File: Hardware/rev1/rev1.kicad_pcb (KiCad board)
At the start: 2 copper layers, 13 parts, among them J1 USB_C_Receptacle_GCT_USB4085, J3 TerminalBlock_MetzConnect_360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, U1 - STM32F103 LQFP-48, U2 SOT-89-3, U3 LGA-8, U4 SOIC-8, Y1 Crystal_SMD

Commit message: hehe did something lol
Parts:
- added C8: C_0402, Capacitor_SMD:C_0402_1005Metric, F.Cu at (117.2, 103.2)
- added C9: C_0402, Capacitor_SMD:C_0402_1005Metric, F.Cu at (126.0, 98.6)
- added D1: D_0402_1005Metric, Diode_SMD:D_0402_1005Metric, F.Cu at (125.6, 94.8)
- added D2: D_0402_1005Metric, Diode_SMD:D_0402_1005Metric, F.Cu at (116.0, 96.8)
- moved GND 77.5 mm to (158.0, 97.3), turned to -90 degrees
- moved J1 64.9 mm to (111.1, 96.0), turned to -90 degrees
- moved R2 59.2 mm to (113.2, 97.8), turned to 180 degrees
- moved R4 56.7 mm to (113.2, 99.4), turned to 180 degrees
- moved C11 44.2 mm to (147.9, 102.3)
- moved U3 42.6 mm to (150.4, 103.5)
- moved R6 37.9 mm to (154.1, 101.4), turned to 180 degrees
- moved R7 35.8 mm to (154.1, 103.2), turned to 180 degrees
- moved J3 32.0 mm to (122.0, 96.2), turned to 180 degrees
- moved U4 25.5 mm to (131.2, 100.7)
- moved U2 24.9 mm to (120.5, 101.4), turned to 90 degrees
- moved U1 - STM32F103 12.7 mm to (141.1, 99.3)
- moved Y1 11.4 mm to (153.6, 98.4)
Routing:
- net (no net): track 165.5 -> 164.8 mm, vias 3 -> 4

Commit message: who actually knows what i have done, daniel says most of it needs work lol
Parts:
- removed C11, C8, C9: C_0402, Capacitor_SMD:C_0402_1005Metric
- removed D1, D2: D_0402_1005Metric, Diode_SMD:D_0402_1005Metric
- removed GND: Battery_Panasonic_CR1025-VSK_Vertical_CircularHoles, Battery:Battery_Panasonic_CR1025-VSK_Vertical_CircularHoles
- removed U1 - STM32F103: LQFP-48, Package_QFP:LQFP-48_7x7mm_P0.5mm
- added C12: 10p, Capacitor_SMD:C_0402_1005Metric, F.Cu at (148.6, 58.7)
- added C13: 10p, Capacitor_SMD:C_0402_1005Metric, F.Cu at (151.2, 62.1)
- added R1: 1k5, Resistor_SMD:R_0402_1005Metric, F.Cu at (123.9, 60.1)
- added R5: 1k5, Resistor_SMD:R_0402_1005Metric, F.Cu at (147.3, 93.4)
- added REF**: BatteryHolder_Keystone_3034_1x20mm, Battery:BatteryHolder_Keystone_3034_1x20mm, B.Cu at (136.8, 109.0)
- added U1: STM32F103C8Tx, Package_QFP:LQFP-48_7x7mm_P0.5mm, F.Cu at (137.0, 109.2)
- J1: value USB_C_Receptacle_GCT_USB4085 -> USB_C_Receptacle_GCT_USB4105-xx-A_16P_TopMnt_Horizontal; footprint Connector_USB:USB_C_Receptacle_GCT_USB4085 -> Connector_USB:USB_C_Receptacle_GCT_USB4105-xx-A_16P_TopMnt_Horizontal
- R2, R4: value R_0402 -> 5k1
- R6, R7: value R_0603 -> 10k; footprint Resistor_SMD:R_0603_1608Metric -> Resistor_SMD:R_0402_1005Metric
- U2: value SOT-89-3 -> HT75xx-1-SOT89
- U3: value LGA-8 -> MS5607-02BA
- U4: value SOIC-8 -> W25Q128JVS
- Y1: value Crystal_SMD -> 16MHz
- moved J1 48.1 mm to (153.8, 118.2), turned to 0 degrees
- moved U3 45.6 mm to (111.6, 79.5)
- moved R2 44.5 mm to (122.3, 54.3), turned to 0 degrees
- moved R7 42.7 mm to (118.3, 79.8), turned to 0 degrees
- moved R6 40.4 mm to (121.9, 77.0), turned to 0 degrees
- moved Y1 40.1 mm to (143.0, 59.7)
- moved R4 33.9 mm to (135.9, 74.3), turned to 0 degrees
- moved U4 33.7 mm to (115.3, 71.0), turned to 0 degrees
- moved J3 31.2 mm to (152.6, 102.1), turned to 0 degrees
- moved U2 29.3 mm to (145.8, 116.3), turned to -90 degrees
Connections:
- R2 pad 1: (no net) -> GND
- R2 pad 2: (no net) -> Net-(J1-CC1)
- R4 pad 1: (no net) -> Net-(J1-CC2)
- R4 pad 2: (no net) -> GND
- R6 pad 1: (no net) -> +3.3V
- R6 pad 2: (no net) -> I2C2_SDA
- R7 pad 1: (no net) -> +3.3V
- R7 pad 2: (no net) -> I2C2_SCK
- U2 pad 1: (no net) -> GND
- U2 pad 2: (no net) -> Net-(J3-Pin_2)
- U2 pad 3: (no net) -> +3V3
- U3 pad 1: (no net) -> +3.3V
- U3 pad 2: (no net) -> +3.3V
- U3 pad 3: (no net) -> GND
- U3 pad 4: (no net) -> GND
- U3 pad 5: (no net) -> GND
- U3 pad 6: (no net) -> unconnected-(U3-SDO-Pad6)
- U3 pad 7: (no net) -> I2C2_SDA
- U3 pad 8: (no net) -> I2C2_SCK
- U4 pad 1: (no net) -> unconnected-(U4-~{CS}-Pad1)
- U4 pad 2: (no net) -> Flash Data Out
- U4 pad 3: (no net) -> unconnected-(U4-IO2-Pad3)
- U4 pad 4: (no net) -> GND
- U4 pad 5: (no net) -> Flash Data In
- U4 pad 6: (no net) -> SPI_CLK
- U4 pad 7: (no net) -> unconnected-(U4-IO3-Pad7)
- U4 pad 8: (no net) -> +3.3V
- Y1 pad 1: (no net) -> HSE_IN
- Y1 pad 2: (no net) -> GND
- Y1 pad 3: (no net) -> GND
- Y1 pad 4: (no net) -> HSE_OUT
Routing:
- net (no net): track 164.8 -> 0.00 mm, vias 4 -> 0
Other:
- board outline added: 50 x 25 mm
- copper layers 2 -> 4

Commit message: UUUUHHH
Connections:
- net System_Reset renamed /MCU et al Sheet/System_Reset
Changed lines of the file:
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@@
 	(net 14 "unconnected-(U1-PA3-Pad13)")
 	(net 15 "unconnected-(U1-PB11-Pad22)")
-	(net 16 "System_Reset")
+	(net 16 "/MCU et al Sheet/System_Reset")
 	(net 17 "NC{slash}TDI_Debug")
 	(net 18 "unconnected-(U1-BOOT0-Pad44)")
@@
 			(layers "F.Cu" "F.Paste" "F.Mask")
 			(roundrect_rratio 0.25)
-			(net 16 "System_Reset")
+			(net 16 "/MCU et al Sheet/System_Reset")
 			(pinfunction "NRST")
 			(pintype "input")
@@
 		(tags "THT single screw terminal block Metz Connect 360272 size 4x4mm^2 drill 1.5mm pad 3mm")
 		(property "Reference" "J3"
-			(at 1.5 -3.06 360)
+			(at 1.5 -3.06 0)
 			(layer "F.SilkS")
 			(effects
@@
 		)
 		(property "Value" "TerminalBlock_MetzConnect_360272_1x01_Horizontal_ScrewM2.6"
-			(at 1.5 3.06 360)
+			(at 1.5 3.06 0)
 			(layer "F.Fab")
 			(hide yes)
@@
 		)
 		(fp_text user "${REFERENCE}"
-			(at 1.5 -3.06 360)
+			(at 1.5 -3.06 0)
 			(layer "F.Fab")
 			(effects
@@
 		)
 		(fp_text user "${REFERENCE}"
-			(at 0.2 0 360)
-			(layer "F.Fab")
-			(effects
+			(at 0.2 0 0)
+			(layer "F.Fab")
+			(effects

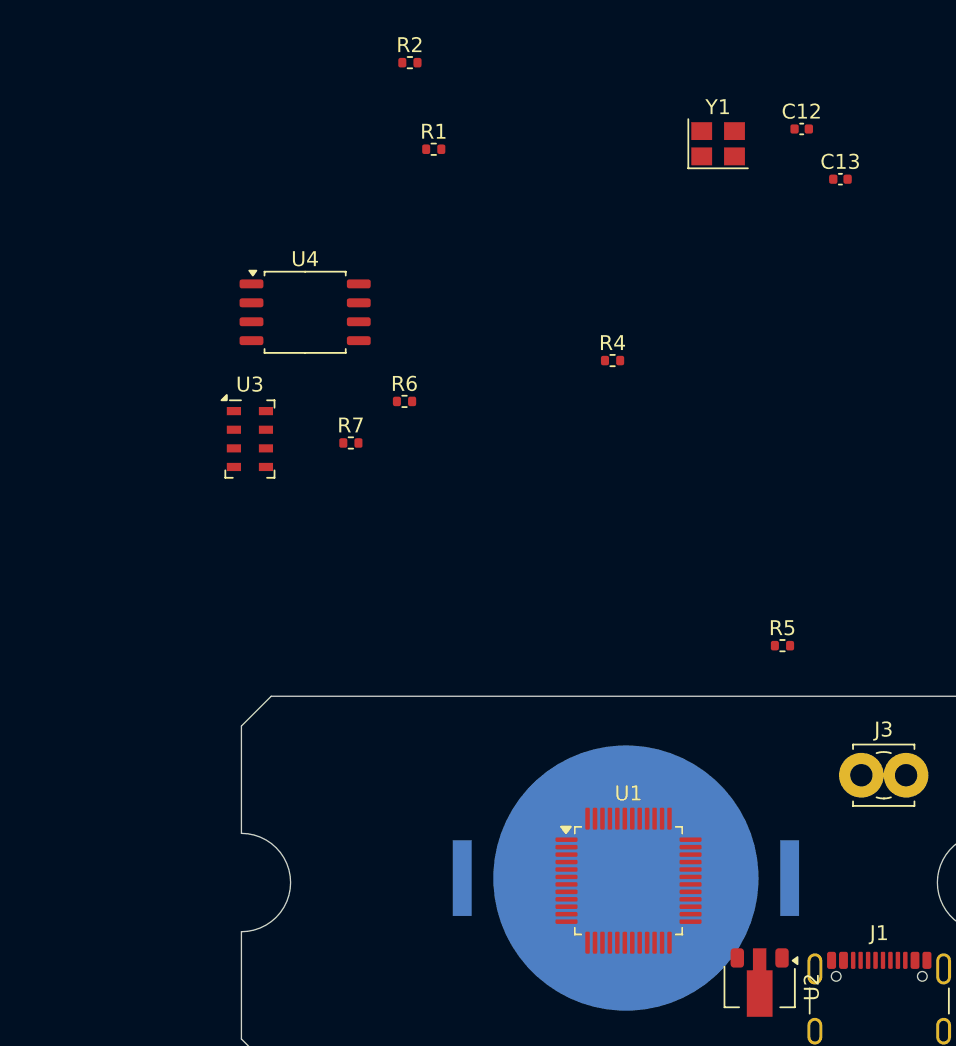
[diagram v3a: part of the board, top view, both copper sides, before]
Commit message: Updated footprints for capacitors
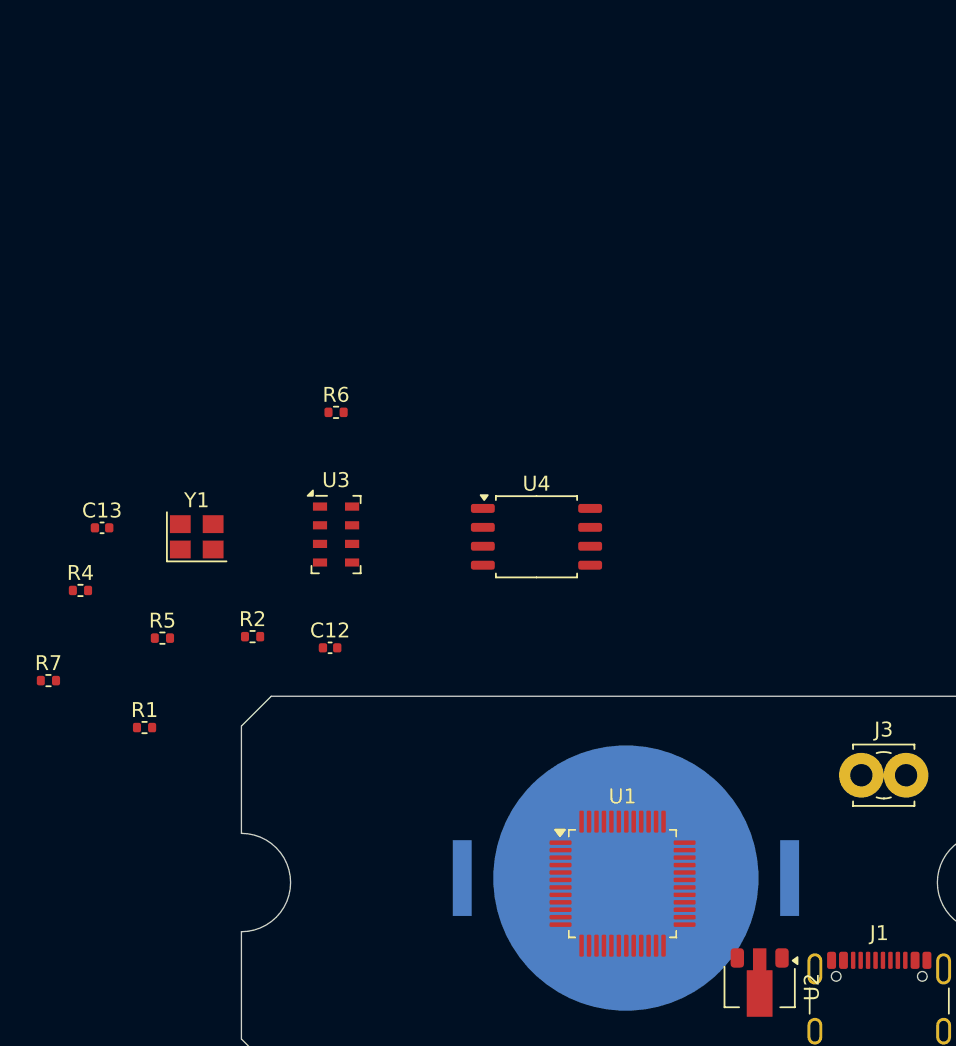
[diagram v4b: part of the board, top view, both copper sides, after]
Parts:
- moved C13 54.8 mm to (101.7, 85.5)
- moved C12 47.0 mm to (117.0, 93.5)
- moved Y1 43.8 mm to (108.0, 86.1)
- moved R1 43.4 mm to (104.5, 98.9)
- moved R5 41.6 mm to (105.7, 92.9)
- moved R2 39.9 mm to (111.8, 92.8)
- moved R4 38.9 mm to (100.2, 89.7)
- moved R7 25.8 mm to (98.0, 95.8)
- moved U4 21.6 mm to (130.8, 86.1)
- moved U3 8.63 mm to (117.3, 86.0)
- moved R6 4.65 mm to (117.3, 77.8)
- moved U1 0.45 mm to (136.6, 109.4)
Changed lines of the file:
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@@
 	(footprint "Capacitor_SMD:C_0402_1005Metric"
 		(layer "F.Cu")
-		(at 148.595 58.735)
+		(at 116.95 93.55)
 		(descr "Capacitor SMD 0402 (1005 Metric), square (rectangular) end terminal, IPC_7351 nominal, (Body size source: IPC-SM-782 page 76, https://www.pcb-3d.com/wordpress/wp-content/uploads/ipc-sm-782a_amendment_1_and_2.pdf), generated with kicad-footprint-generator")
 		(tags "capacitor")
@@
 	(footprint "Resistor_SMD:R_0402_1005Metric"
 		(layer "F.Cu")
-		(at 122.305 54.285)
+		(at 111.75 92.8)
 		(descr "Resistor SMD 0402 (1005 Metric), square (rectangular) end terminal, IPC_7351 nominal, (Body size source: IPC-SM-782 page 72, https://www.pcb-3d.com/wordpress/wp-content/uploads/ipc-sm-782a_amendment_1_and_2.pdf), generated with kicad-footprint-generator")
 		(tags "resistor")
@@
 	(footprint "Package_QFP:LQFP-48_7x7mm_P0.5mm"
 		(layer "F.Cu")
-		(at 136.975 109.175)
+		(at 136.575 109.375)
 		(descr "LQFP, 48 Pin (https://www.analog.com/media/en/technical-documentation/data-sheets/ltc2358-16.pdf), generated with kicad-footprint-generator ipc_gullwing_generator.py")
 		(tags "LQFP QFP")
 		(property "Reference" "U1"
-			(at 0 -5.85 0)
+			(at 0 -5.85 360)
 			(layer "F.SilkS")
 			(effects
@@
 		)
 		(property "Value" "STM32F103C8Tx"
-			(at 0 5.85 0)
+			(at 0 5.85 360)
 			(layer "F.Fab")
 			(effects
@@
 		)
 		(fp_text user "${REFERENCE}"
-			(at 0 0 0)
+			(at 0 0 360)
 			(layer "F.Fab")
 			(effects
@@
 	(footprint "Resistor_SMD:R_0402_1005Metric"
 		(layer "F.Cu")
-		(at 118.345 79.805)
+		(at 98.05 95.75)
 		(descr "Resistor SMD 0402 (1005 Metric), square (rectangular) end terminal, IPC_7351 nominal, (Body size source: IPC-SM-782 page 72, https://www.pcb-3d.com/wordpress/wp-content/uploads/ipc-sm-782a_amendment_1_and_2.pdf), generated with kicad-footprint-generator")
 		(tags "resistor")
@@
 	(footprint "Resistor_SMD:R_0402_1005Metric"
 		(layer "F.Cu")
-		(at 123.905 60.095)
+		(at 104.5 98.9)
 		(descr "Resistor SMD 0402 (1005 Metric), square (rectangular) end terminal, IPC_7351 nominal, (Body size source: IPC-SM-782 page 72, https://www.pcb-3d.com/wordpress/wp-content/uploads/ipc-sm-782a_amendment_1_and_2.pdf), generated with kicad-footprint-generator")
 		(tags "resistor")
@@
 	(footprint "Capacitor_SMD:C_0402_1005Metric"
 		(layer "F.Cu")
-		(at 151.195 62.105)
+		(at 101.65 85.5)
 		(descr "Capacitor SMD 0402 (1005 Metric), square (rectangular) end terminal, IPC_7351 nominal, (Body size source: IPC-SM-782 page 76, https://www.pcb-3d.com/wordpress/wp-content/uploads/ipc-sm-782a_amendment_1_and_2.pdf), generated with kicad-footprint-generator")
 		(tags "capacitor")
@@
 	(footprint "Resistor_SMD:R_0402_1005Metric"
 		(layer "F.Cu")
-		(at 121.945 77.015)
+		(at 117.35 77.75)
 		(descr "Resistor SMD 0402 (1005 Metric), square (rectangular) end terminal, IPC_7351 nominal, (Body size source: IPC-SM-782 page 72, https://www.pcb-3d.com/wordpress/wp-content/uploads/ipc-sm-782a_amendment_1_and_2.pdf), generated with kicad-footprint-generator")
 		(tags "resistor")
@@
 	(footprint "Package_SO:SOIC-8_5.23x5.23mm_P1.27mm"
 		(layer "F.Cu")
-		(at 115.275 71.035)
+		(at 130.8 86.1)
 		(descr "SOIC, 8 Pin (http://www.winbond.com/resource-files/w25q32jv%20revg%2003272018%20plus.pdf#page=68), generated with kicad-footprint-generator ipc_gullwing_generator.py")
 		(tags "SOIC SO")
@@
 	(footprint "Resistor_SMD:R_0402_1005Metric"
 		(layer "F.Cu")
-		(at 135.905 74.275)
+		(at 100.2 89.7)
 		(descr "Resistor SMD 0402 (1005 Metric), square (rectangular) end terminal, IPC_7351 nominal, (Body size source: IPC-SM-782 page 72, https://www.pcb-3d.com/wordpress/wp-content/uploads/ipc-sm-782a_amendment_1_and_2.pdf), generated with kicad-footprint-generator")
 		(tags "resistor")
@@
 	(footprint "Package_LGA:LGA-8_3x5mm_P1.25mm"
 		(layer "F.Cu")
-		(at 111.57 79.54)
+		(at 117.35 85.95)
 		(descr "LGA-8")
 		(tags "lga land grid array")
@@
 	(footprint "Crystal:Crystal_SMD_3225-4Pin_3.2x2.5mm"
 		(layer "F.Cu")
-		(at 142.985 59.725)
+		(at 108 86.1)
 		(descr "SMD Crystal SERIES SMD3225/4 http://www.txccrystal.com/images/pdf/7m-accuracy.pdf, 3.2x2.5mm^2 package")
 		(tags "SMD SMT crystal")
@@
 	(footprint "Resistor_SMD:R_0402_1005Metric"
 		(layer "F.Cu")
-		(at 147.305 93.405)
+		(at 105.7 92.9)
 		(descr "Resistor SMD 0402 (1005 Metric), square (rectangular) end terminal, IPC_7351 nominal, (Body size source: IPC-SM-782 page 72, https://www.pcb-3d.com/wordpress/wp-content/uploads/ipc-sm-782a_amendment_1_and_2.pdf), generated with kicad-footprint-generator")
 		(tags "resistor")

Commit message: Revert "Updated footprints for capacitors"
This reverts commit 54b9e5590742c75ae1802e9536bdc0a5b115109b.
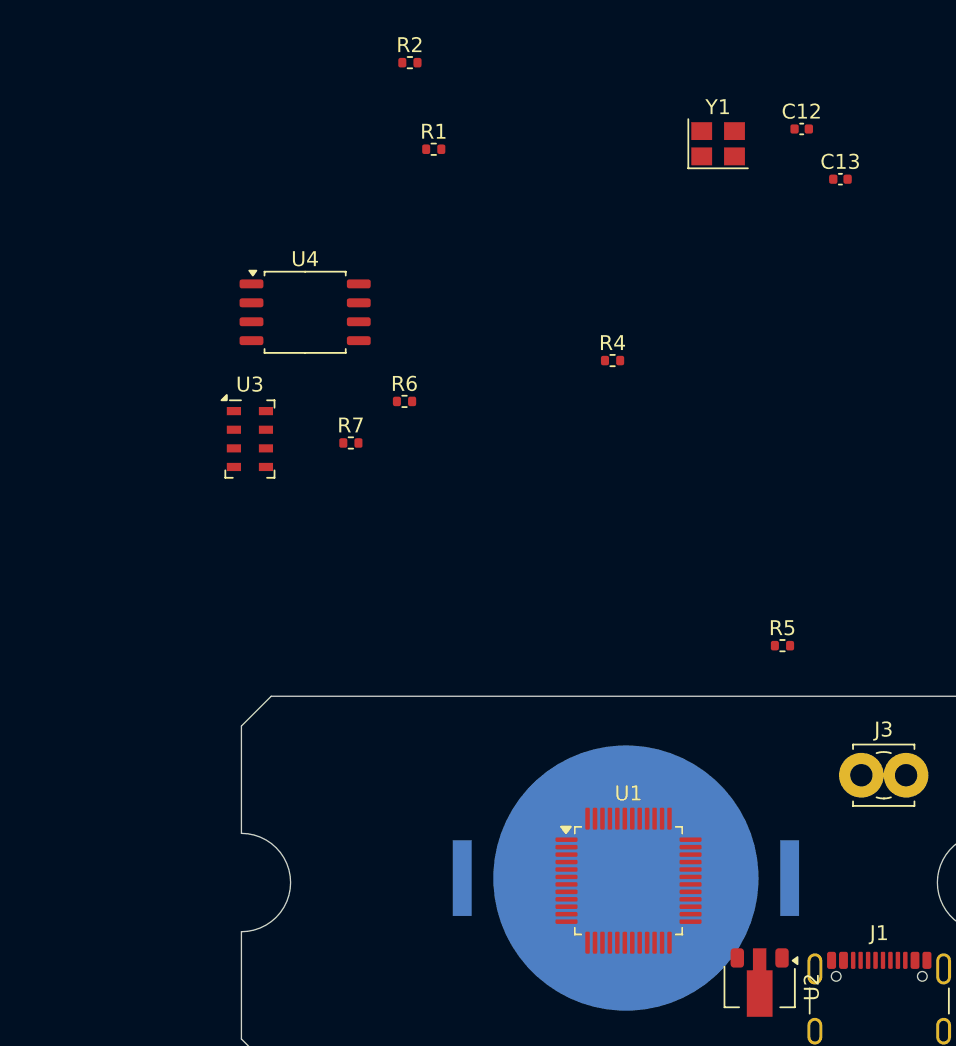
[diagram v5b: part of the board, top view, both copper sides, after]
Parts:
- moved C13 54.8 mm to (151.2, 62.1)
- moved C12 47.0 mm to (148.6, 58.7)
- moved Y1 43.8 mm to (143.0, 59.7)
- moved R1 43.4 mm to (123.9, 60.1)
- moved R5 41.6 mm to (147.3, 93.4)
- moved R2 39.9 mm to (122.3, 54.3)
- moved R4 38.9 mm to (135.9, 74.3)
- moved R7 25.8 mm to (118.3, 79.8)
- moved U4 21.6 mm to (115.3, 71.0)
- moved U3 8.63 mm to (111.6, 79.5)
- moved R6 4.65 mm to (121.9, 77.0)
- moved U1 0.45 mm to (137.0, 109.2)
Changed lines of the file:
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@@
 	(footprint "Capacitor_SMD:C_0402_1005Metric"
 		(layer "F.Cu")
-		(at 116.95 93.55)
+		(at 148.595 58.735)
 		(descr "Capacitor SMD 0402 (1005 Metric), square (rectangular) end terminal, IPC_7351 nominal, (Body size source: IPC-SM-782 page 76, https://www.pcb-3d.com/wordpress/wp-content/uploads/ipc-sm-782a_amendment_1_and_2.pdf), generated with kicad-footprint-generator")
 		(tags "capacitor")
@@
 	(footprint "Resistor_SMD:R_0402_1005Metric"
 		(layer "F.Cu")
-		(at 111.75 92.8)
+		(at 122.305 54.285)
 		(descr "Resistor SMD 0402 (1005 Metric), square (rectangular) end terminal, IPC_7351 nominal, (Body size source: IPC-SM-782 page 72, https://www.pcb-3d.com/wordpress/wp-content/uploads/ipc-sm-782a_amendment_1_and_2.pdf), generated with kicad-footprint-generator")
 		(tags "resistor")
@@
 	(footprint "Package_QFP:LQFP-48_7x7mm_P0.5mm"
 		(layer "F.Cu")
-		(at 136.575 109.375)
+		(at 136.975 109.175)
 		(descr "LQFP, 48 Pin (https://www.analog.com/media/en/technical-documentation/data-sheets/ltc2358-16.pdf), generated with kicad-footprint-generator ipc_gullwing_generator.py")
 		(tags "LQFP QFP")
 		(property "Reference" "U1"
-			(at 0 -5.85 360)
+			(at 0 -5.85 0)
 			(layer "F.SilkS")
 			(effects
@@
 		)
 		(property "Value" "STM32F103C8Tx"
-			(at 0 5.85 360)
+			(at 0 5.85 0)
 			(layer "F.Fab")
 			(effects
@@
 		)
 		(fp_text user "${REFERENCE}"
-			(at 0 0 360)
+			(at 0 0 0)
 			(layer "F.Fab")
 			(effects
@@
 	(footprint "Resistor_SMD:R_0402_1005Metric"
 		(layer "F.Cu")
-		(at 98.05 95.75)
+		(at 118.345 79.805)
 		(descr "Resistor SMD 0402 (1005 Metric), square (rectangular) end terminal, IPC_7351 nominal, (Body size source: IPC-SM-782 page 72, https://www.pcb-3d.com/wordpress/wp-content/uploads/ipc-sm-782a_amendment_1_and_2.pdf), generated with kicad-footprint-generator")
 		(tags "resistor")
@@
 	(footprint "Resistor_SMD:R_0402_1005Metric"
 		(layer "F.Cu")
-		(at 104.5 98.9)
+		(at 123.905 60.095)
 		(descr "Resistor SMD 0402 (1005 Metric), square (rectangular) end terminal, IPC_7351 nominal, (Body size source: IPC-SM-782 page 72, https://www.pcb-3d.com/wordpress/wp-content/uploads/ipc-sm-782a_amendment_1_and_2.pdf), generated with kicad-footprint-generator")
 		(tags "resistor")
@@
 	(footprint "Capacitor_SMD:C_0402_1005Metric"
 		(layer "F.Cu")
-		(at 101.65 85.5)
+		(at 151.195 62.105)
 		(descr "Capacitor SMD 0402 (1005 Metric), square (rectangular) end terminal, IPC_7351 nominal, (Body size source: IPC-SM-782 page 76, https://www.pcb-3d.com/wordpress/wp-content/uploads/ipc-sm-782a_amendment_1_and_2.pdf), generated with kicad-footprint-generator")
 		(tags "capacitor")
@@
 	(footprint "Resistor_SMD:R_0402_1005Metric"
 		(layer "F.Cu")
-		(at 117.35 77.75)
+		(at 121.945 77.015)
 		(descr "Resistor SMD 0402 (1005 Metric), square (rectangular) end terminal, IPC_7351 nominal, (Body size source: IPC-SM-782 page 72, https://www.pcb-3d.com/wordpress/wp-content/uploads/ipc-sm-782a_amendment_1_and_2.pdf), generated with kicad-footprint-generator")
 		(tags "resistor")
@@
 	(footprint "Package_SO:SOIC-8_5.23x5.23mm_P1.27mm"
 		(layer "F.Cu")
-		(at 130.8 86.1)
+		(at 115.275 71.035)
 		(descr "SOIC, 8 Pin (http://www.winbond.com/resource-files/w25q32jv%20revg%2003272018%20plus.pdf#page=68), generated with kicad-footprint-generator ipc_gullwing_generator.py")
 		(tags "SOIC SO")
@@
 	(footprint "Resistor_SMD:R_0402_1005Metric"
 		(layer "F.Cu")
-		(at 100.2 89.7)
+		(at 135.905 74.275)
 		(descr "Resistor SMD 0402 (1005 Metric), square (rectangular) end terminal, IPC_7351 nominal, (Body size source: IPC-SM-782 page 72, https://www.pcb-3d.com/wordpress/wp-content/uploads/ipc-sm-782a_amendment_1_and_2.pdf), generated with kicad-footprint-generator")
 		(tags "resistor")
@@
 	(footprint "Package_LGA:LGA-8_3x5mm_P1.25mm"
 		(layer "F.Cu")
-		(at 117.35 85.95)
+		(at 111.57 79.54)
 		(descr "LGA-8")
 		(tags "lga land grid array")
@@
 	(footprint "Crystal:Crystal_SMD_3225-4Pin_3.2x2.5mm"
 		(layer "F.Cu")
-		(at 108 86.1)
+		(at 142.985 59.725)
 		(descr "SMD Crystal SERIES SMD3225/4 http://www.txccrystal.com/images/pdf/7m-accuracy.pdf, 3.2x2.5mm^2 package")
 		(tags "SMD SMT crystal")
@@
 	(footprint "Resistor_SMD:R_0402_1005Metric"
 		(layer "F.Cu")
-		(at 105.7 92.9)
+		(at 147.305 93.405)
 		(descr "Resistor SMD 0402 (1005 Metric), square (rectangular) end terminal, IPC_7351 nominal, (Body size source: IPC-SM-782 page 72, https://www.pcb-3d.com/wordpress/wp-content/uploads/ipc-sm-782a_amendment_1_and_2.pdf), generated with kicad-footprint-generator")
 		(tags "resistor")
